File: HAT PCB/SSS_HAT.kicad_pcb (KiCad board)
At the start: 2 copper layers, 30.8 x 76.6 mm, 27 parts, among them J1 ESP32_Connector_0, J2 ESP32_Connector_1, J3 CAN, J4 CAN, J5 I2C, J6 ADC_0, J7 ADC_1, U1 TJA1051T, U2 MCP3422Axx-xMS, U3 ICM-42688-P

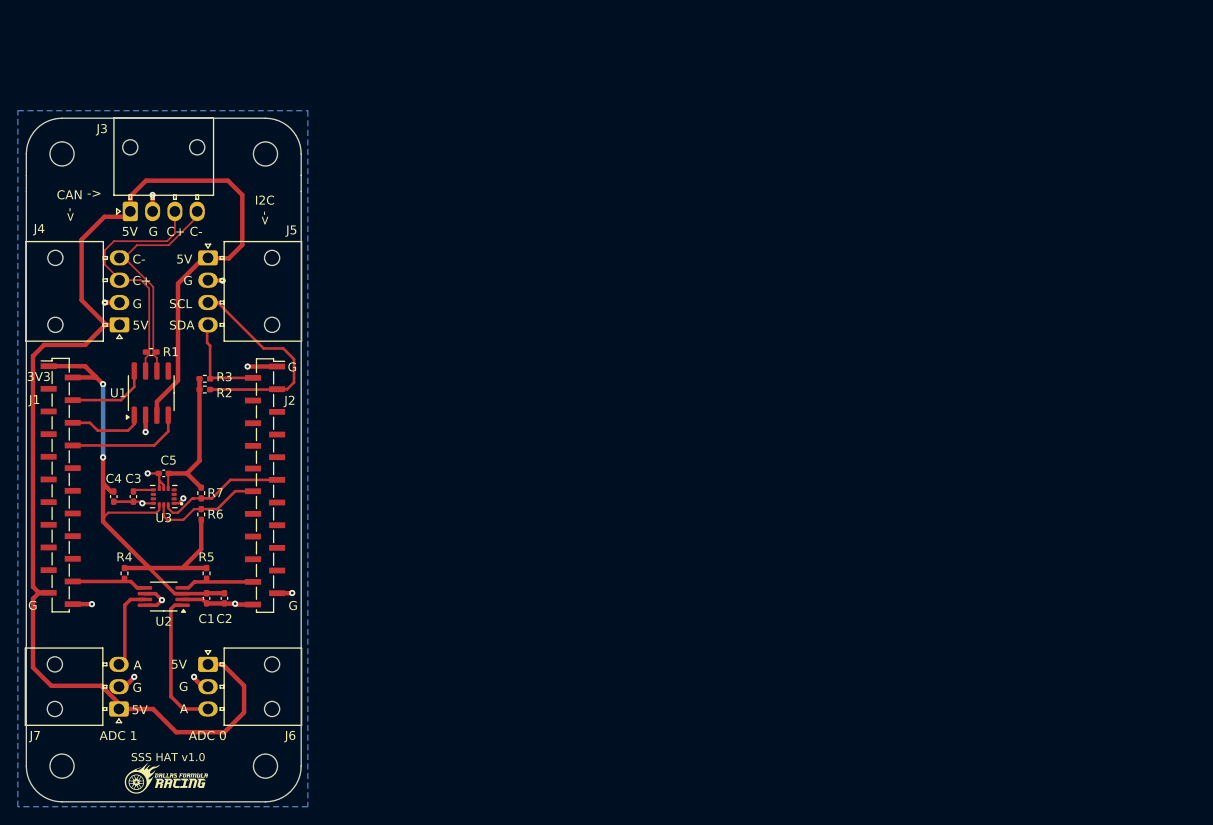
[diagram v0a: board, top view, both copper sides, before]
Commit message: Replaced ADC for ADS8320EB-250, changed molex connectors to hirose connectors and re-routed PCB
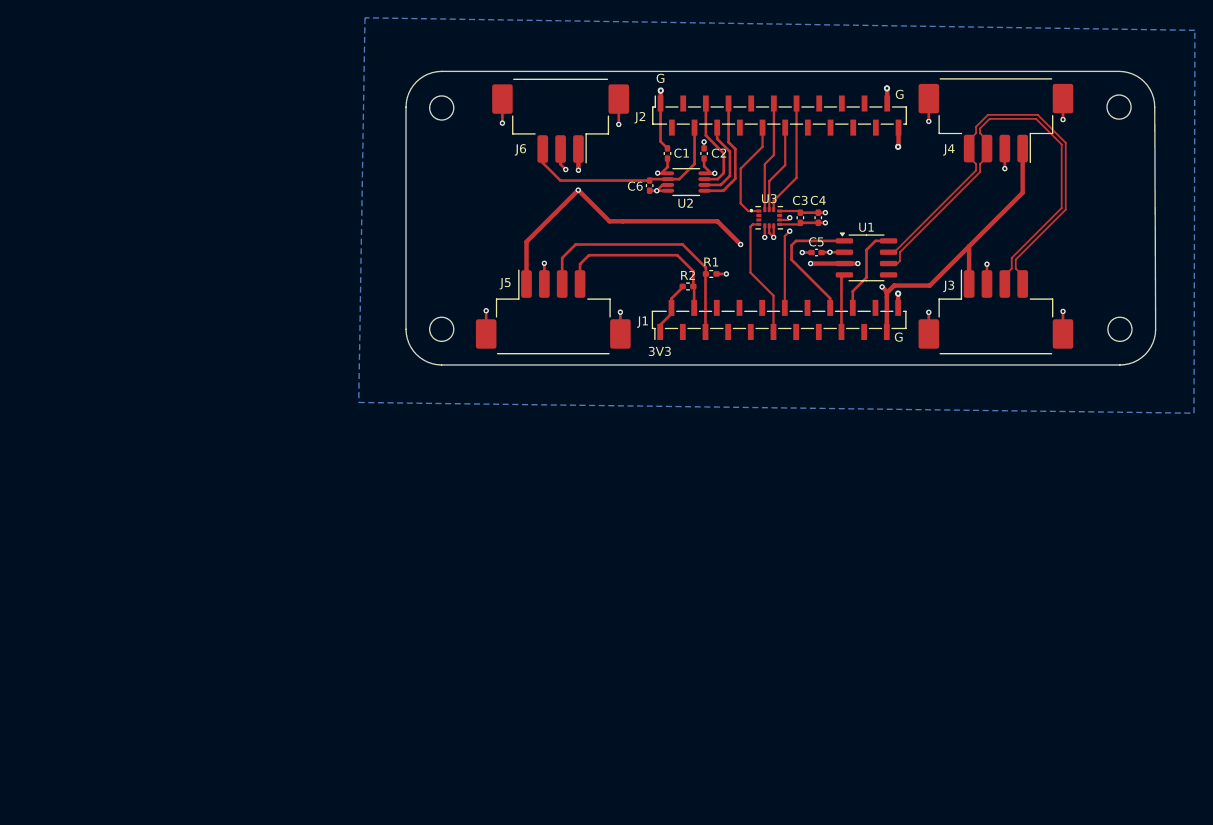
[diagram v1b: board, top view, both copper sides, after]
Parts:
- removed G***: LOGO, LOGO
- removed J7: ADC_1, Connector_Molex:Molex_Nano-Fit_105313-xx03_1x03_P2.50mm_Horizontal
- removed R3, R6, R7: 10k, Resistor_SMD:R_0402_1005Metric_Pad0.72x0.64mm_HandSolder
- removed R4, R5: 2k2, Resistor_SMD:R_0402_1005Metric_Pad0.72x0.64mm_HandSolder
- added C6: 1μF, Capacitor_SMD:C_0402_1005Metric_Pad0.74x0.62mm_HandSolder, F.Cu at (103.3, 40.9)
- C1: value 0.1μF -> 10μF
- C2: value 10μF -> 1μF
- J3, J4: value CAN -> I2C; footprint Connector_Molex:Molex_Nano-Fit_105313-xx04_1x04_P2.50mm_Horizontal -> Connector_Hirose:Hirose_DF3EA-04P-2H_1x04-1MP_P2.00mm_Horizontal
- J5: footprint Connector_Molex:Molex_Nano-Fit_105313-xx04_1x04_P2.50mm_Horizontal -> Connector_Hirose:Hirose_DF3EA-04P-2H_1x04-1MP_P2.00mm_Horizontal
- J6: value ADC_0 -> ADC; footprint Connector_Molex:Molex_Nano-Fit_105313-xx03_1x03_P2.50mm_Horizontal -> Connector_Hirose:Hirose_DF3EA-03P-2H_1x03-1MP_P2.00mm_Horizontal
- R1: value 120 -> 10k
- U2: value MCP3422Axx-xMS -> ADS8320EB_250; footprint Package_SO:MSOP-8_3x3mm_P0.65mm -> ADS8320EB_250:DGK0008A_L
- moved H4 139.6 mm to (155.9, 32.1)
- moved H1 120.2 mm to (156.0, 57.0)
- moved J4 100.8 mm to (142.1, 33.9)
- moved J3 97.6 mm to (142.1, 54.8), turned to 0 degrees
- moved C4 84.9 mm to (122.2, 44.5), turned to -90 degrees
- moved J1 82.6 mm to (117.8, 56.0), turned to 90 degrees
- moved U1 81.6 mm to (127.6, 49.0), turned to 0 degrees
- moved C3 81.0 mm to (120.2, 44.5), turned to -90 degrees
- moved C5 77.2 mm to (122.0, 48.4), turned to 0 degrees
- moved U2 74.7 mm to (107.4, 40.5), turned to 0 degrees
- moved U3 74.7 mm to (116.7, 44.5), turned to 0 degrees
- moved C2 73.3 mm to (109.4, 37.3), turned to 90 degrees
- moved J6 72.3 mm to (93.3, 34.0), turned to 180 degrees
- moved C1 71.8 mm to (105.3, 37.3), turned to 90 degrees
- moved J2 71.0 mm to (117.9, 33.0), turned to 90 degrees
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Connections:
- net IMU_SDA renamed IMU_MOSI
- J1 pad 11: unconnected-(J1-Pin_11-Pad11) -> IMU_INT1
- J1 pad 12: unconnected-(J1-Pin_12-Pad12) -> IMU_INT2
- J1 pad 16: unconnected-(J1-Pin_16-Pad16) -> CAN_TX
- J1 pad 17: unconnected-(J1-Pin_17-Pad17) -> CAN_RX
- J1 pad 18: unconnected-(J1-Pin_18-Pad18) -> CAN_S
- J1 pad 20: ADC_SCL -> unconnected-(J1-Pin_20-Pad20)
- J1 pad 4: CAN_S -> I2C_SDA
- J1 pad 5: unconnected-(J1-Pin_5-Pad5) -> I2C_SCL
- J1 pad 6: CAN_TX -> unconnected-(J1-Pin_6-Pad6)
- J1 pad 8: CAN_RX -> unconnected-(J1-Pin_8-Pad8)
- J2 pad 10: unconnected-(J2-Pin_10-Pad10) -> IMU_MISO
- J2 pad 13: unconnected-(J2-Pin_13-Pad13) -> IMU_CS
- J2 pad 2: I2C_SDA -> unconnected-(J2-Pin_2-Pad2)
- J2 pad 20: ADC_SDA -> unconnected-(J2-Pin_20-Pad20)
- J2 pad 3: I2C_SCL -> unconnected-(J2-Pin_3-Pad3)
- J2 pad 4: unconnected-(J2-Pin_4-Pad4) -> A_In
- J2 pad 5: unconnected-(J2-Pin_5-Pad5) -> A_SCL
- J2 pad 6: unconnected-(J2-Pin_6-Pad6) -> A_SDA
- J2 pad 7: unconnected-(J2-Pin_7-Pad7) -> A_CS
- J3 pad 3: CAN+ -> CAN-
- J3 pad 4: CAN- -> CAN+
- J4 pad 3: CAN+ -> CAN-
- J4 pad 4: CAN- -> CAN+
- J6 pad 3: ADC_0 -> A_In
- R1 pad 1: CAN- -> +3.3V
- R1 pad 2: CAN+ -> I2C_SCL
- R2 pad 2: I2C_SCL -> I2C_SDA
- U2 pad 1: ADC_0 -> +3.3V
- U2 pad 2: GND -> A_In
- U2 pad 3: +3.3V -> GND
- U2 pad 4: ADC_SDA -> GND
- U2 pad 5: ADC_SCL -> A_CS
- U2 pad 6: GND -> A_SDA
- U2 pad 7: ADC_1 -> A_SCL
- U2 pad 8: GND -> +3.3V
- U3 pad 1: GND -> IMU_MISO
- U3 pad 12: +3.3V -> IMU_CS
- U3 pad 4: unconnected-(U3-INT1/INT-Pad4) -> IMU_INT1
- U3 pad 9: unconnected-(U3-INT2/FSYNC/CLKIN-Pad9) -> IMU_INT2
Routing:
- net +3.3V: track 85.8 -> 20.9 mm, vias 2 -> 6
- net +5V: track 148.2 -> 90.4 mm, vias 0 -> 6
- net CAN-: track 24.3 -> 49.7 mm
- net A_In: track 0.00 -> 24.2 mm
- net CAN+: track 27.6 -> 49.5 mm
- net ADC_0: track 15.4 -> 0.00 mm
- net GND: track 41.5 -> 56.9 mm, vias 14 -> 21
- net IMU_INT1: track 0.00 -> 13.9 mm
- net IMU_CS: track 0.00 -> 12.9 mm
- net A_CS: track 0.00 -> 12.7 mm
- net IMU_MISO: track 0.00 -> 11.9 mm
- net IMU_INT2: track 0.00 -> 11.6 mm, vias 0 -> 2
- net A_SCL: track 0.00 -> 11.1 mm
- net I2C_SDA: track 10.7 -> 20.2 mm
- net A_SDA: track 0.00 -> 9.27 mm
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- added copper zone on B.Cu, net +3.3V
- added copper zone on In2.Cu, net GND
- removed copper zone on B.Cu, net GND
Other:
- board size 30.8 x 76.6 mm -> 84 x 32.9 mm
- copper layers 2 -> 4
- board text added: "U3"
- board text removed: "->"
- board text removed: "5V"
- board text removed: "A"
- board text removed: "ADC 0"
- board text removed: "ADC 1"
- board text removed: "C+"
- board text removed: "C-"
- board text removed: "CAN"
- board text removed: "I2C"
- board text removed: "SCL"
- board text removed: "SDA"
- board text removed: "SSS HAT v1.0"

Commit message: Updated 3D model & readme.
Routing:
- net +3.3V: track 20.9 -> 22.3 mm, vias 6 -> 7
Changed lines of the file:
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@@
 		(tags "resistor handsolder")
 		(property "Reference" "R1"
-			(at 0 1.3 360)
+			(at 0 1.3 0)
 			(layer "F.SilkS")
 			(effects
@@
 		)
 		(property "Value" "10k"
-			(at 0 1.17 360)
+			(at 0 1.17 0)
 			(layer "F.Fab")
 			(effects
@@
 		)
 		(fp_text user "${REFERENCE}"
-			(at 0 0 360)
+			(at 0 0 0)
 			(layer "F.Fab")
 			(effects
@@
 		(tags "resistor handsolder")
 		(property "Reference" "R2"
-			(at 0 -1.2 360)
+			(at 0 -1.2 0)
 			(layer "F.SilkS")
 			(effects
@@
 		)
 		(property "Value" "10k"
-			(at 0 1.17 360)
+			(at 0 1.17 0)
 			(layer "F.Fab")
 			(effects
@@
 		)
 		(fp_text user "${REFERENCE}"
-			(at 0 0 360)
+			(at 0 0 0)
 			(layer "F.Fab")
 			(effects
@@
 		)
 		(property "Value" "I2C"
-			(at 0 6.05 360)
+			(at 0 6.05 0)
 			(layer "F.Fab")
 			(effects
@@
 		)
 		(fp_text user "${REFERENCE}"
-			(at 0 1.9 360)
+			(at 0 1.9 0)
 			(layer "F.Fab")
 			(effects
@@
 			(pintype "passive")
 		)
-		(model "${KICAD8_3DMODEL_DIR}/Connector_Hirose.3dshapes/Hirose_DF3EA-04P-2H_1x04-1MP_P2.00mm_Horizontal.wrl"
+		(model "${KIPRJMOD}/Connectors/DF3EA-4P-2H(24).STEP"
 			(offset
-				(xyz 0 0 0)
+				(xyz 0 1 2.6)
 			)
 			(scale
@@
 			)
 			(rotate
-				(xyz 0 0 0)
+				(xyz 90 0 180)
 			)
 		)
@@
 		)
 		(fp_text user "${REFERENCE}"
-			(at 0 0 360)
+			(at 0 0 0)
 			(layer "F.Fab")
 			(effects
@@
 		)
 		(property "Footprint" "ADS8320EB_250:DGK0008A_L"
-			(at 0 0 360)
+			(at 0 0 0)
 			(layer "F.Fab")
 			(hide yes)
@@
 		)
 		(property "Datasheet" ""
-			(at 0 0 360)
+			(at 0 0 0)
 			(layer "F.Fab")
 			(hide yes)
@@
 		)
 		(property "Description" ""
-			(at 0 0 360)
+			(at 0 0 0)
 			(layer "F.Fab")
 			(hide yes)
@@
 		(fp_arc
 			(start 1.375443 -1.495814)
-			(mid 1.462519 -1.458647)
+			(mid 1.462485 -1.458641)
 			(end 1.499675 -1.371582)
 			(stroke
@@
 			(pintype "power_in")
 		)
+		(model "${KIPRJMOD}/ADC/DGK0008A.stp"
+			(offset
+				(xyz 0 0 0)
+			)
+			(scale
+				(xyz 1 1 1)
+			)
+			(rotate
+				(xyz 0 0 0)
+			)
+		)
 	)
 	(footprint "MountingHole:MountingHole_2.7mm_M2.5"
@@
 		)
 		(property "Value" "I2C"
-			(at 0 6.05 360)
+			(at 0 6.05 0)
 			(layer "F.Fab")
 			(effects
@@
 		)
 		(fp_text user "${REFERENCE}"
-			(at 0 1.9 360)
+			(at 0 1.9 0)
 			(layer "F.Fab")
 			(effects
@@
 			(pintype "passive")
 		)
-		(model "${KICAD8_3DMODEL_DIR}/Connector_Hirose.3dshapes/Hirose_DF3EA-04P-2H_1x04-1MP_P2.00mm_Horizontal.wrl"
+		(model "${KIPRJMOD}/Connectors/DF3EA-4P-2H(24).STEP"
 			(offset
-				(xyz 0 0 0)
+				(xyz 0 1 2.6)
 			)
 			(scale
@@
 			)
 			(rotate
-				(xyz 0 0 0)
+				(xyz 90 0 180)
 			)
 		)
@@
 		)
 		(property "Value" "I2C"
-			(at 0 6.05 360)
+			(at 0 6.05 0)
 			(layer "F.Fab")
 			(effects
@@
 		)
 		(fp_text user "${REFERENCE}"
-			(at 0 1.9 360)
+			(at 0 1.9 0)
 			(layer "F.Fab")
 			(effects
@@
 			(pintype "passive")
 		)
-		(model "${KICAD8_3DMODEL_DIR}/Connector_Hirose.3dshapes/Hirose_DF3EA-04P-2H_1x04-1MP_P2.00mm_Horizontal.wrl"
+		(model "${KIPRJMOD}/Connectors/DF3EA-4P-2H(24).STEP"
 			(offset
-				(xyz 0 0 0)
+				(xyz 0 1 2.6)
 			)
 			(scale
@@
 			)
 			(rotate
-				(xyz 0 0 0)
+				(xyz 90 0 180)
 			)
 		)
@@
 		)
 		(fp_text user "${REFERENCE}"
-			(at 0 0 360)
+			(at 0 0 0)
 			(layer "F.Fab")
 			(effects
@@
 		)
 		(property "Value" "ADC"
-			(at 0 6.05 360)
+			(at 0 6.05 0)
 			(layer "F.Fab")
 			(effects
@@
 		)
 		(fp_text user "${REFERENCE}"
-			(at 0 1.9 360)
+			(at 0 1.9 0)
 			(layer "F.Fab")
 			(effects
@@
 			(pintype "passive")
 		)
-		(model "${KICAD8_3DMODEL_DIR}/Connector_Hirose.3dshapes/Hirose_DF3EA-03P-2H_1x03-1MP_P2.00mm_Horizontal.wrl"
+		(model "${KIPRJMOD}/Connectors/DF3EA-3P-2H(51).STEP"
 			(offset
-				(xyz 0 0 0)
+				(xyz 0 1 2.6)
 			)
 			(scale
@@
 			)
 			(rotate
-				(xyz 0 0 0)
+				(xyz 90 0 180)
 			)
 		)
@@
 				(font
 					(size 0.48 0.48)
-					(thickness 0.15)
+					(thickness 0.12)
 				)
 			)
@@
 				(font
 					(size 0.48 0.48)
-					(thickness 0.15)
+					(thickness 0.12)
 				)
 			)
@@
 			(pintype "bidirectional")
 		)
+		(model "${KIPRJMOD}/IMU/ICM-42688-P.step"
+			(offset
+				(xyz 0 0 0.001)
+			)
+			(scale
+				(xyz 1 1 1)
+			)
+			(rotate
+				(xyz -90 0 0)
+			)
+		)
 	)
 	(gr_line
@@
 	)
 	(segment
+		(start 107.0025 51.8025)
+		(end 107.0025 52.2)
+		(width 0.3)
+		(layer "F.Cu")
+		(net 11)
+	)
+	(segment
 		(start 105.3 37.8675)
 		(end 105.3 38.824998)
@@
 	)
 	(segment
+		(start 106.3 51.1)
+		(end 107.0025 51.8025)
+		(width 0.3)
+		(layer "F.Cu")
+		(net 11)
+	)
+	(segment
 		(start 104.475 56.525)
 		(end 105.745 55.255)
@@
 		(size 0.6)
 		(drill 0.3)
+		(layers "F.Cu" "B.Cu")
+		(net 11)
+	)
+	(via
+		(at 106.3 51.1)
+		(size 0.6)
+		(drill 0.3)
